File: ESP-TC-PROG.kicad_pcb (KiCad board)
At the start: 2 copper layers, 37.6 x 16.1 mm, 22 parts, among them J1 USB, J2 TC, J3 PINH, Q1 AO3400A, Q2 AO3400A, Q3 AO3401A, U1 USBLC6-4, U2 CH340G, Y1 12Mhz

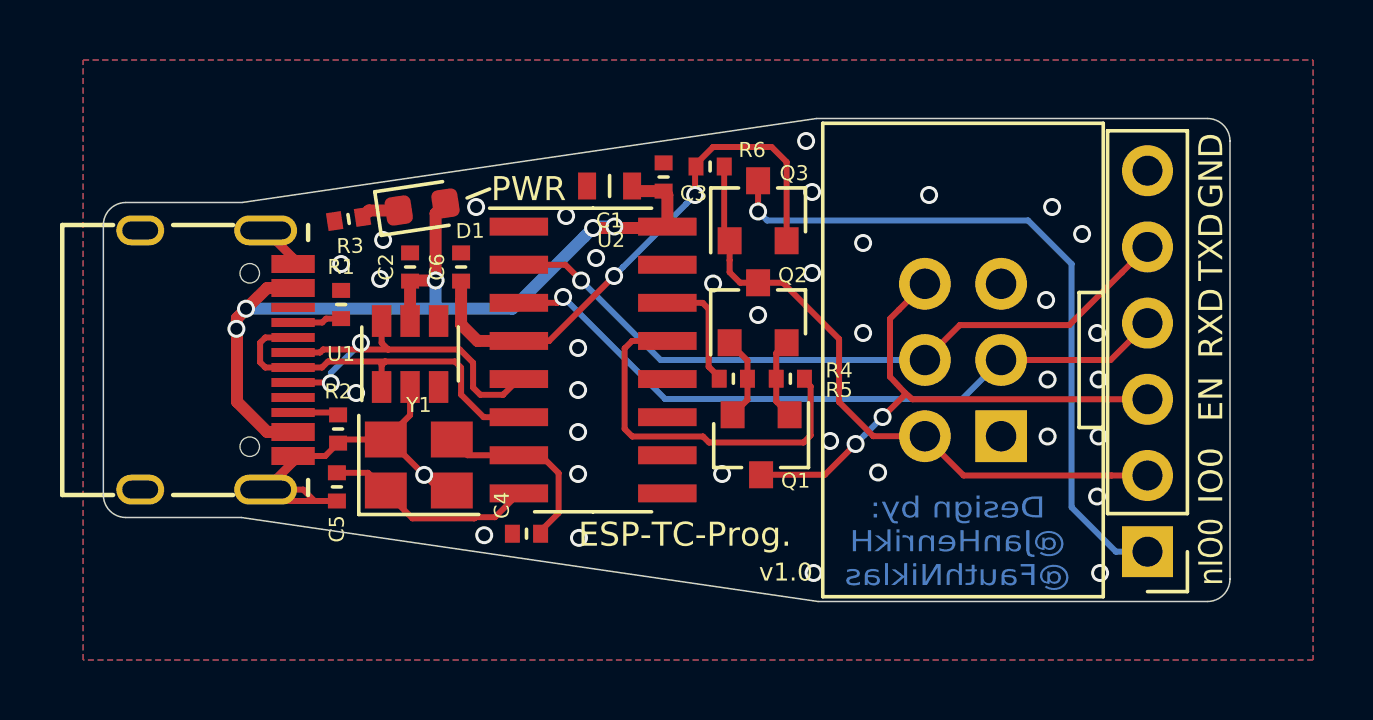
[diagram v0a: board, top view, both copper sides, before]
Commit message: updated files to kicad 6
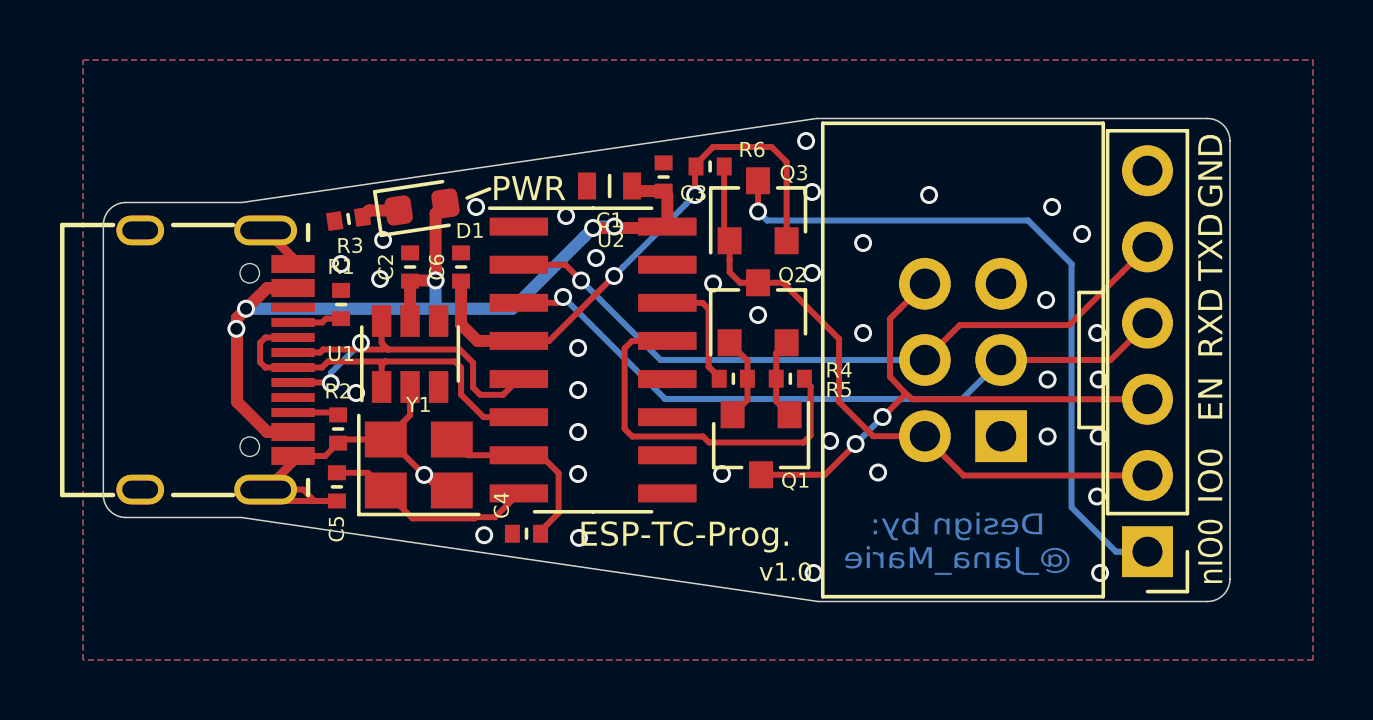
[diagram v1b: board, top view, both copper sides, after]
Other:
- net class Default removed
- board text added: "Design by: @_Jana_Marie"
- board text removed: "Design by: @JanHenrikH @FauthNiklas"

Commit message: updated to v1.2.1
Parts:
- removed Q3: AO3401A, Package_TO_SOT_SMD:SOT-23
- added R7: 5k1, otter:R_0402, F.Cu at (122.5, 96.2)
- C1: value 10µ -> 4u7; footprint otter:C_0603 -> otter:C_0805
- C2, C3, C6: value 0.1µ -> 100n
- Q1, Q2: value AO3400A -> S8050-J3Y
- R6: value 100k -> 5k1
- U2: value CH340G -> CH340G/C
- moved R6 11.7 mm to (122.6, 105.1)
- moved C3 1.35 mm to (120.7, 94.0)
- moved C1 1.05 mm to (118.6, 94.1)
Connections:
- J1 pad A8: Net-(J1-PadA8) -> unconnected-(J1-PadA8)
- J1 pad B8: Net-(J1-PadB8) -> unconnected-(J1-PadB8)
- J2 pad 1: Net-(J2-Pad1) -> unconnected-(J2-Pad1)
- J3 pad 1: nIO0 -> unconnected-(J3-Pad1)
- Q2 pad 1: Net-(Q1-Pad2) -> Net-(Q2-Pad1)
- Q2 pad 2: Net-(Q1-Pad1) -> Net-(Q2-Pad2)
- R4 pad 2: Net-(R4-Pad2) -> Net-(Q2-Pad2)
- R5 pad 1: Net-(Q1-Pad2) -> Net-(Q2-Pad1)
- R5 pad 2: Net-(R5-Pad2) -> Net-(Q1-Pad2)
- R6 pad 2: IO0 -> EN
- U1 pad 3: Net-(U1-Pad3) -> unconnected-(U1-Pad3)
- U1 pad 4: Net-(U1-Pad4) -> unconnected-(U1-Pad4)
- U2 pad 10: Net-(U2-Pad10) -> unconnected-(U2-Pad10)
- U2 pad 11: Net-(U2-Pad11) -> unconnected-(U2-Pad11)
- U2 pad 12: Net-(U2-Pad12) -> unconnected-(U2-Pad12)
- U2 pad 13: Net-(R4-Pad2) -> Net-(Q2-Pad2)
- U2 pad 14: Net-(R5-Pad2) -> Net-(Q1-Pad2)
- U2 pad 15: Net-(U2-Pad15) -> unconnected-(U2-Pad15)
- U2 pad 9: Net-(U2-Pad9) -> unconnected-(U2-Pad9)
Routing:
- net nIO0: track 23.5 -> 0.00 mm, vias 1 -> 0
- net Net-(Q2-Pad2): track 0.00 -> 14.1 mm
- net Net-(R4-Pad2): track 12.7 -> 0.00 mm
- net V3: track 18.6 -> 24.6 mm
- net Net-(R5-Pad2): track 3.93 -> 0.00 mm
- net IO0: track 21.6 -> 18.3 mm
- net Net-(Q1-Pad2): track 2.85 -> 5.32 mm
- net EN: track 18.4 -> 19.9 mm
- net Net-(Q2-Pad1): track 0.00 -> 1.45 mm
- net Net-(Q1-Pad1): track 2.73 -> 1.38 mm
- net VBUS: track 32.3 -> 33.7 mm
- net GND: vias 36 -> 30
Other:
- board text added: "USB-UART"
- board text added: "USB-UART-BRIDGE 2023 v1.2.1 @jana@mystical.garden"
- board text removed: "Design by: @_Jana_Marie"
- board text removed: "ESP-TC-Prog."
- board text removed: "nIO0"
- board text removed: "v1.0"
